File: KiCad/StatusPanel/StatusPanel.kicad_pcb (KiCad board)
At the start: 2 copper layers, 121 x 92 mm, 53 parts, among them J1 CONN, J10 CONN_12V_CTL, J11 CONN_12V_GND, J12 CONN_TASK_CTL, J13 CONN_TASK_GND, J14 CONN_5V_CTL, J15 CONN_5V_GND, J16 CONN_COM_CTL, J17 CONN_COM_GND, J18 CONN_LOW_CTL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

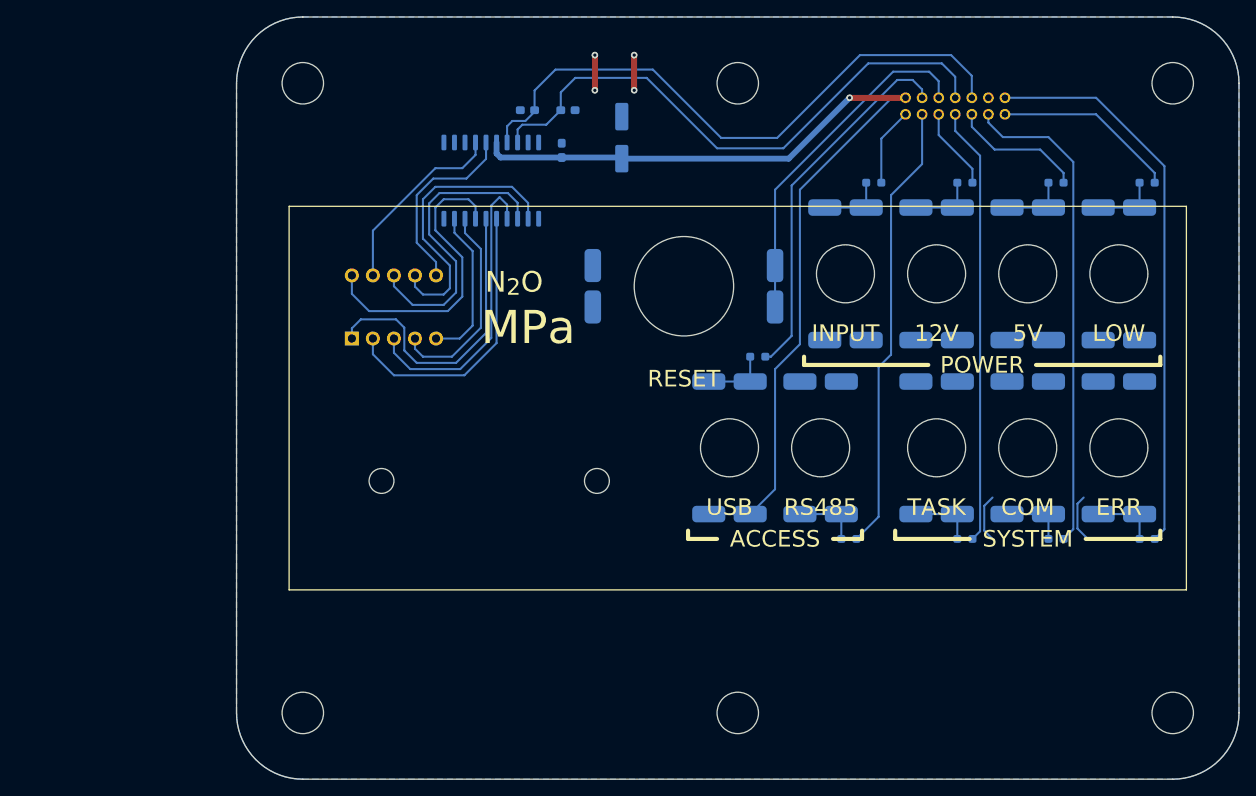
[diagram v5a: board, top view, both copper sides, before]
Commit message: ステータスパネルのコネクタをDF11に変更
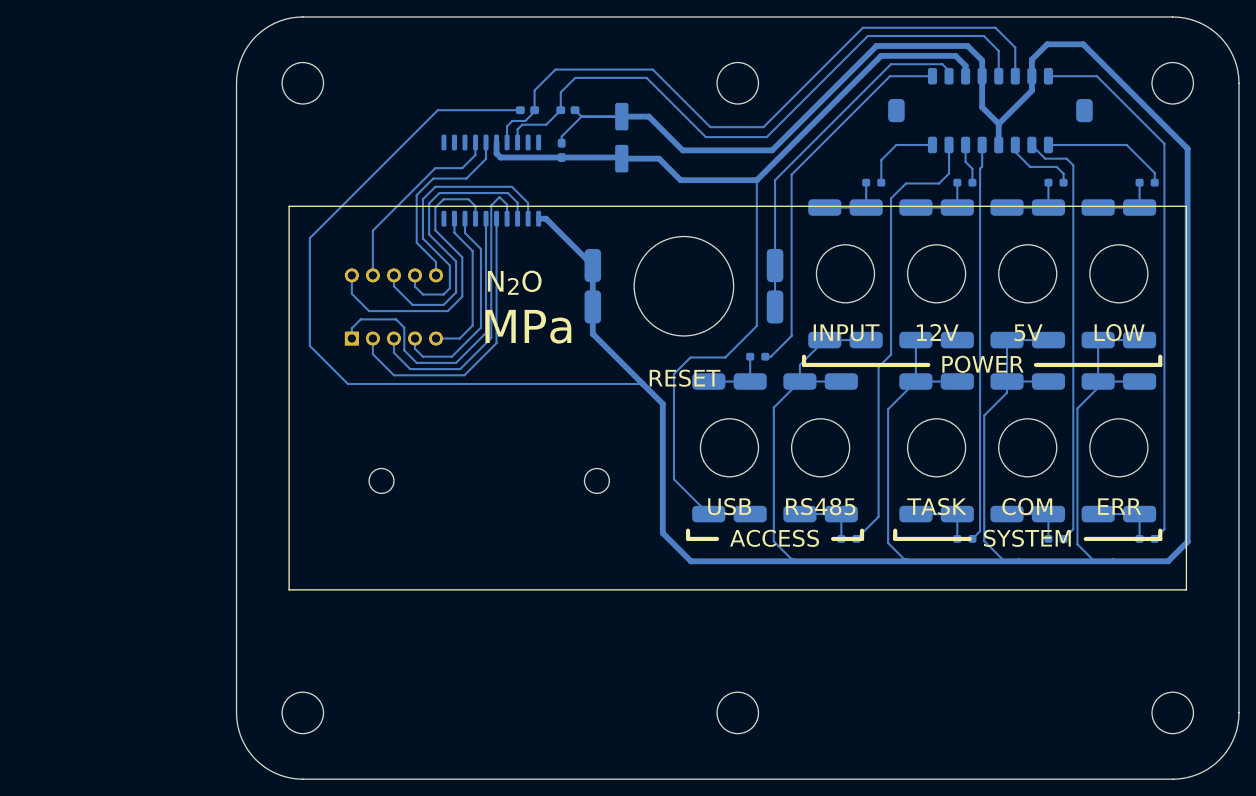
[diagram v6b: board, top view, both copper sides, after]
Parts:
- J1: footprint TSRP_Connector_Hirose:DF51A-14DP-2DS -> TSRP_Connector_Hirose:DF11CZ-16DP-2V
- moved J1 10.3 mm to (174.3, 55.2)
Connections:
- J1 pad 10: DIO -> CLK
- J1 pad 11: COM -> 5V
- J1 pad 12: GND -> DIO
- J1 pad 13: LOW -> COM
- J1 pad 14: ERROR -> GND
- J1 pad 2: +5V -> USB
- J1 pad 4: USB -> RESET
- J1 pad 6: RESET -> +5V
- J1 pad 8: CLK -> GND
- J1 pad 9: 5V -> GND
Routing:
- net GND: track 20.2 -> 516.9 mm, vias 4 -> 0
- net COM: track 59.2 -> 51.6 mm
- net 5V: track 16.1 -> 8.84 mm
- net LOW: track 22.2 -> 15.4 mm
- net DIO: track 73.6 -> 79.9 mm
- net CLK: track 69.2 -> 75.3 mm
- net 12V: track 9.94 -> 4.89 mm
- net TASK: track 52.9 -> 48.0 mm
- net +5V: track 118.1 -> 121.0 mm, vias 1 -> 0
- net ERROR: track 68.2 -> 65.6 mm
- net RESET: track 42.3 -> 43.1 mm
- net USB: track 44.9 -> 45.6 mm
- removed copper zone on B.Cu, net GND

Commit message: ステータスパネルをビルド
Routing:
- net 5V: track 8.84 -> 7.99 mm
- net GND: track 516.9 -> 516.1 mm
- net RESET: track 43.1 -> 42.4 mm
- net Net-(U1-C): track 36.2 -> 35.6 mm
